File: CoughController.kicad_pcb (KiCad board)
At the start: 2 copper layers, 99 x 85 mm, 51 parts, among them J3 AUDIO IN/OUT, J4 DIO-2, J5 GPIO-OUT, J6 GPIO-IN, J9 Conn_02x04_Odd_Even, K1 G6A-274P-ST-US DC12, K2 G6A-274P-ST-US DC12, U1 TLP627-2, U2 TLP627-2, U3 TLP627-2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

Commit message: bugfix GPIO/IN ドライ接点へ修正
GPIO/INはドライ接点
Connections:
- C1 pad 2: MCOM1 -> GND
- C2 pad 2: MCOM1 -> GND
- J4 pad 9: MCOM1 -> GND
- J6 pad 1: GPIO-IN/1M -> GND
- J6 pad 11: GPIO-IN/5M -> GND
- J6 pad 12: GPIO-IN/6M -> GND
- J6 pad 13: GPIO-IN/7M -> GND
- J6 pad 14: GPIO-IN/8M -> GND
- J6 pad 2: GPIO-IN/2M -> GND
- J6 pad 3: GPIO-IN/3M -> GND
- J6 pad 4: GPIO-IN/4M -> GND
- J9 pad 1: MCOM1 -> GND
- J9 pad 5: MCOM1 -> GND
- R17 pad 2: GPIO-IN/1P -> COM0
- R18 pad 2: GPIO-IN/2P -> COM0
- R19 pad 2: GPIO-IN/3P -> COM0
- R20 pad 2: GPIO-IN/4P -> COM0
- R21 pad 2: GPIO-IN/6P -> COM0
- R22 pad 2: GPIO-IN/5P -> COM0
- R23 pad 2: GPIO-IN/8P -> COM0
- R24 pad 2: GPIO-IN/7P -> COM0
- U5 pad 2: GPIO-IN/1M -> GPIO-IN/2P
- U5 pad 4: GPIO-IN/2M -> GPIO-IN/1P
- U5 pad 5: MCOM1 -> GND
- U5 pad 6: DIO-2/IN2 -> DIO-2/IN1
- U5 pad 7: MCOM1 -> GND
- U5 pad 8: DIO-2/IN1 -> DIO-2/IN2
- U6 pad 2: GPIO-IN/3M -> GPIO-IN/4P
- U6 pad 4: GPIO-IN/4M -> GPIO-IN/3P
- U6 pad 5: MCOM1 -> GND
- U6 pad 6: DIO-2/IN4 -> DIO-2/IN3
- U6 pad 7: MCOM1 -> GND
- U6 pad 8: DIO-2/IN3 -> DIO-2/IN4
- locked pad 1: MCOM1 -> GND (x3)
- locked pad 13: MCOM1 -> GND
- locked pad 17: MCOM1 -> GND
- locked pad 5: MCOM1 -> GND (x3)
- locked pad 9: MCOM1 -> GND (x2)
- locked pad 2: GPIO-IN/7M -> GPIO-IN/8P
- locked pad 4: GPIO-IN/8M -> GPIO-IN/7P
- locked pad 6: DIO-2/IN8 -> DIO-2/IN7
- locked pad 7: MCOM1 -> GND (x2)
- locked pad 8: DIO-2/IN7 -> DIO-2/IN8
- locked pad 2: GPIO-IN/5M -> GPIO-IN/6P
- locked pad 4: GPIO-IN/6M -> GPIO-IN/5P
- locked pad 6: DIO-2/IN6 -> DIO-2/IN5
- locked pad 8: DIO-2/IN5 -> DIO-2/IN6
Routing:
- net COM0: track 328.9 -> 393.6 mm
- net GPIO-IN/7M: track 28.7 -> 0.00 mm
- net GPIO-IN/3M: track 28.0 -> 0.00 mm
- net GPIO-IN/8M: track 27.3 -> 0.00 mm
- net GPIO-IN/6M: track 23.9 -> 0.00 mm
- net GPIO-IN/5M: track 23.8 -> 0.00 mm
- net GPIO-IN/4M: track 23.6 -> 0.00 mm
- net GPIO-IN/2M: track 21.4 -> 0.00 mm
- net GPIO-IN/1M: track 19.6 -> 0.00 mm
- net GPIO-IN/1P: track 8.81 -> 23.5 mm
- net GPIO-IN/4P: track 5.98 -> 19.8 mm
- net GPIO-IN/6P: track 6.23 -> 20.0 mm
- net GPIO-IN/8P: track 12.5 -> 25.9 mm
- net GPIO-IN/2P: track 9.53 -> 19.9 mm
- net GPIO-IN/3P: track 13.4 -> 21.3 mm
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- added copper zone on B.Cu, net GND
- added copper zone on F.Cu, net GND
- removed copper zone on B.Cu, net MCOM1
- removed copper zone on F.Cu, net MCOM1

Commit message: rename Symbol and Footprint of relay.
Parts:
- K1, K2: value G6A-274P-ST-US DC12 -> G6A-274P-DC5; footprint SnapLibrary:RELAY_G6A-274P-ST-US DC3_OMR -> SnapLibrary:RELAY_G6A-274P-DC5
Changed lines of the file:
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@@
     )
   )
-  (footprint "SnapLibrary:RELAY_G6A-274P-ST-US DC3_OMR" (layer "F.Cu")
+  (footprint "SnapLibrary:RELAY_G6A-274P-DC5" (layer "F.Cu")
     (at 111.9 128.69 90)
     (tags "G6A-274P-ST-US DC12 ")
@@
         (effects (font (size 1 1) (thickness 0.15)))
     )
-    (fp_text value "G6A-274P-ST-US DC12" (at -3.81 -8.8 90 unlocked) (layer "F.Fab")
+    (fp_text value "G6A-274P-DC5" (at -3.81 -8.8 90 unlocked) (layer "F.Fab")
         (effects (font (size 1 1) (thickness 0.15)))
     )
     (fp_text user "${REFERENCE}" (at -3.81 -8.8 90 unlocked) (layer "F.Fab")
-        (effects (font (size 1 1) (thickness 0.15)))
-    )
-    (fp_text user "*" (at 0 -20.986667 90 unlocked) (layer "F.Fab")
         (effects (font (size 1 1) (thickness 0.15)))
     )
@@
     )
   )
-  (footprint "SnapLibrary:RELAY_G6A-274P-ST-US DC3_OMR" (layer "F.Cu")
+  (footprint "SnapLibrary:RELAY_G6A-274P-DC5" (layer "F.Cu")
     (at 112 113.44 90)
     (tags "G6A-274P-ST-US DC12 ")
@@
         (effects (font (size 1 1) (thickness 0.15)))
     )
-    (fp_text value "G6A-274P-ST-US DC12" (at -3.81 -8.8 90 unlocked) (layer "F.Fab")
-        (effects (font (size 1 1) (thickness 0.15)))
-    )
-    (fp_text user "*" (at -7.62 -20.986667 90 unlocked) (layer "F.Fab")
-        (effects (font (size 1 1) (thickness 0.15)))
-    )
+    (fp_text value "G6A-274P-DC5" (at -3.81 -8.8 90 unlocked) (layer "F.Fab")
+        (effects (font (size 1 1) (thickness 0.15)))
+    )

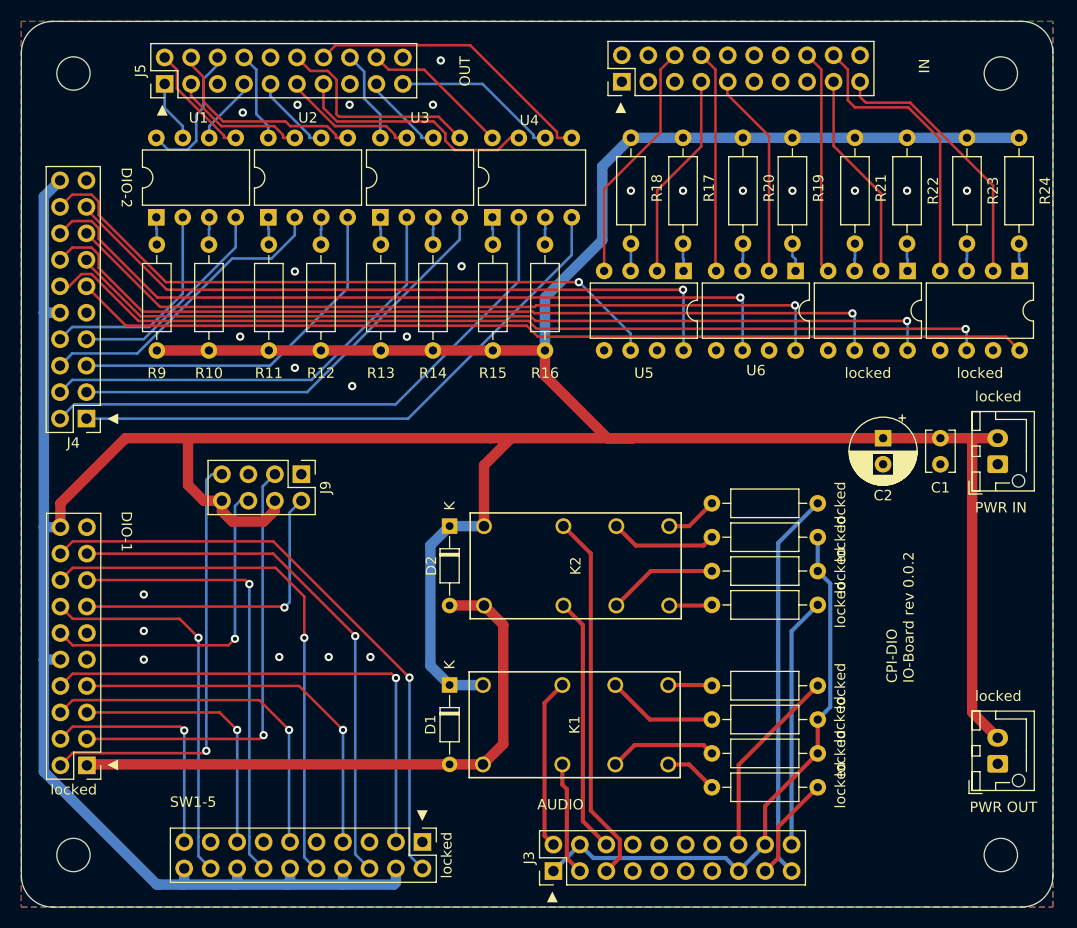
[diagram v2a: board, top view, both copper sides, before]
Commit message: fix footprint of relay
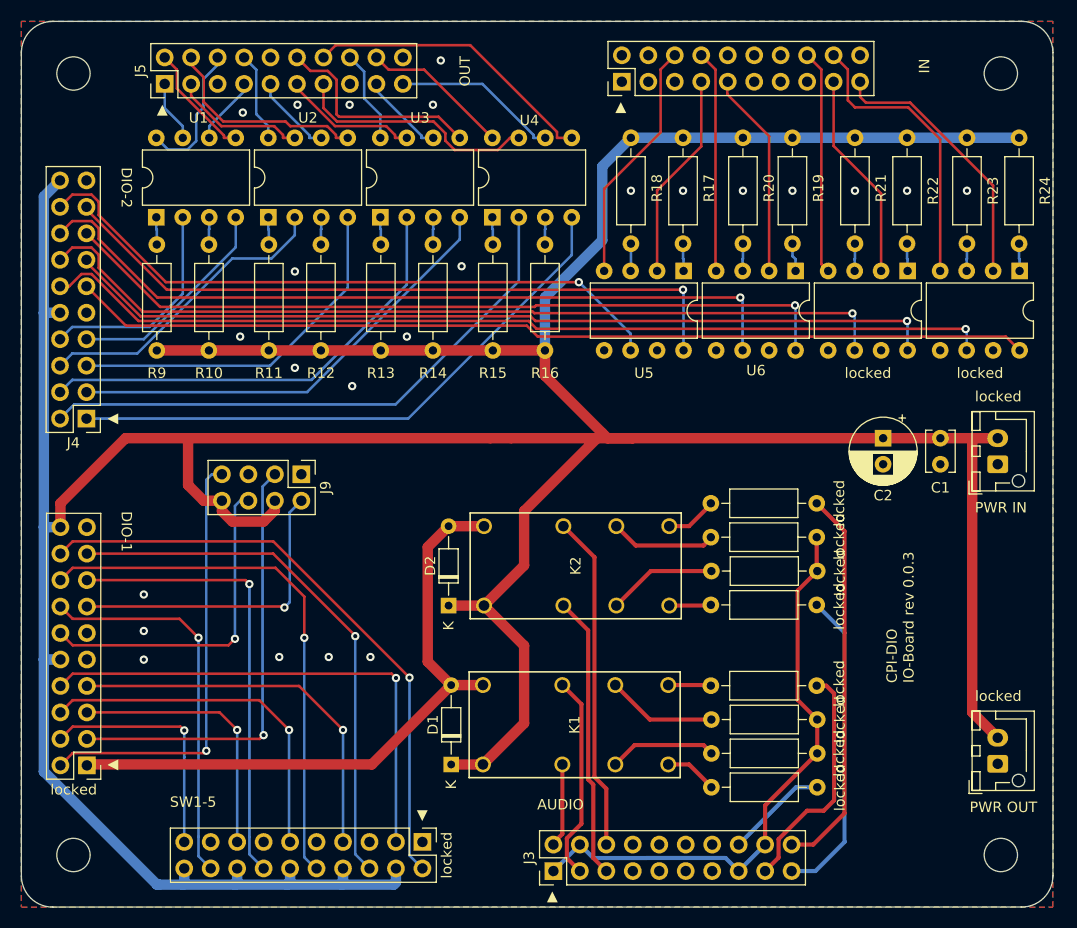
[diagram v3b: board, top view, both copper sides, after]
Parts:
- moved locked 9.75 mm to (126.3, 121.0)
- moved locked 9.75 mm to (126.3, 128.8)
- moved locked 9.75 mm to (116.2, 111.2)
- moved locked 9.75 mm to (116.2, 138.5)
- moved D1 7.63 mm to (91.2, 136.3), turned to 90 degrees
- moved D2 7.63 mm to (91.0, 121.1), turned to 90 degrees
- moved locked 3.25 mm to (116.2, 114.5)
- moved locked 3.25 mm to (126.4, 117.8)
- moved locked 3.25 mm to (126.4, 135.2)
- moved locked 3.25 mm to (116.2, 132.0)
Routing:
- net COM0: track 393.6 -> 407.0 mm
- net AUDIO-OUT-R-COLD: track 24.0 -> 37.2 mm
- net AUDIO-OUT-L-COLD: track 10.1 -> 22.7 mm
- net AUDIO-IN-L-COLD: track 10.9 -> 19.7 mm
- net AUDIO-IN-R-HOT: track 35.9 -> 27.2 mm
- net AUDIO-OUT-L-HOT: track 18.4 -> 9.82 mm
- net AUDIO-IN-L-HOT: track 16.4 -> 8.05 mm
- net AUDIO-IN-R-COLD: track 24.6 -> 32.3 mm
- net AUDIO-OUT-R-HOT: track 37.4 -> 30.1 mm
- net RY_POW: track 58.2 -> 61.6 mm
- net Net-(K2-Pad8): track 5.00 -> 4.01 mm
- net Net-(K1-Pad9): track 5.10 -> 4.11 mm
- net Net-(K2-Pad9): track 4.11 -> 5.00 mm
- net Net-(K1-Pad8): track 4.21 -> 5.10 mm
- net AUDIO-IN-L-GND: track 56.1 -> 56.6 mm
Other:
- board text added: "CPI-DIO IO-Board rev 0.0.3"
- board text removed: "CPI-DIO IO-Board rev 0.0.2"
